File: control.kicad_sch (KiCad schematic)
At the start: 27 parts, among them J7 USB_C_Receptacle_USB2.0, J8 Conn_01x04_Male, J9 Conn_ARM_JTAG_SWD_10, U5 AMS1117-3.3, U6 STM32F042C4Tx, U7 USBLC6-2SC6

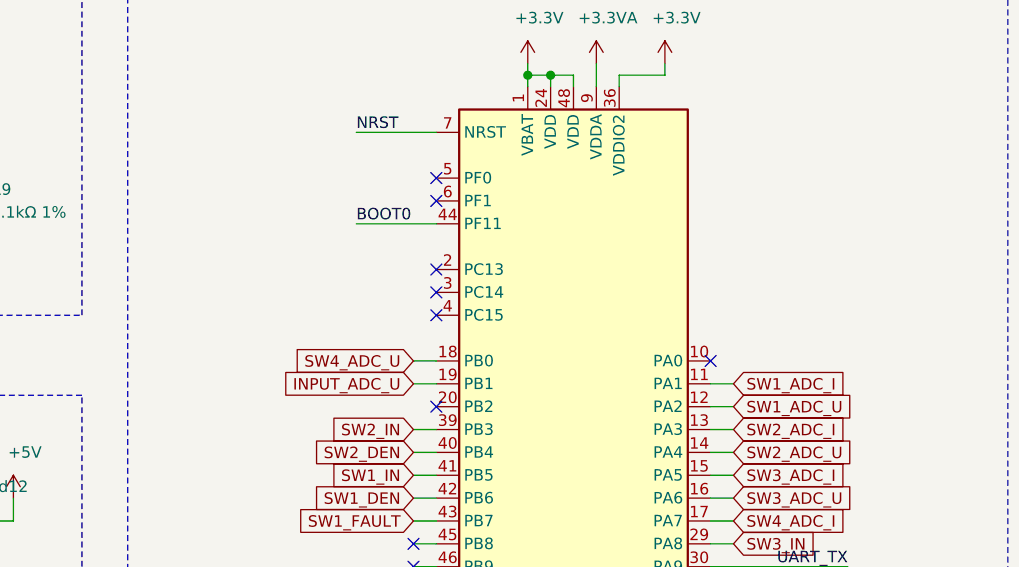
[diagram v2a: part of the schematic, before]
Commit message: add uC controlled status LED, improve filling zones, move LED closer to connectors
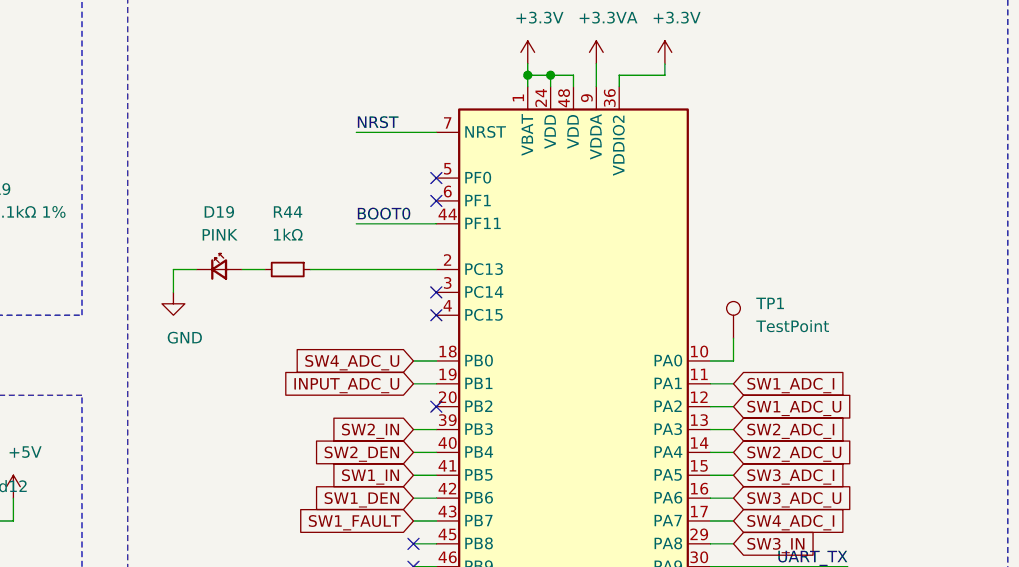
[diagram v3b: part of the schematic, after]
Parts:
- added D19: PINK, LED_SMD:LED_0603_1608Metric, symbol Device:LED_Small
- added R44: 1kΩ, Resistor_SMD:R_0603_1608Metric, symbol Device:R_Small
- added TP1: TestPoint, TestPoint:TestPoint_Pad_D1.0mm, symbol Connector:TestPoint
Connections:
- net GND: now also D19.1 (K)
- net at U6.10 (PA0): now also TP1.1
- net at U6.2 (PC13): now also R44.1
- new net: D19.2 (A), R44.2
- no-connect marks 15 -> 13
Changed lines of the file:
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@@
   (paper "A4")
   (title_block
+    (date "2020-11-09")
+    (rev "v0.1")
     (comment 4 "Author: Stefan Agner")
   )
@@
   (junction (at 209.55 66.04) (diameter 1.016) (color 0 0 0 0))
   (junction (at 212.09 142.24) (diameter 1.016) (color 0 0 0 0))
+  (no_connect (at 227.33 129.54))
+  (no_connect (at 100.33 127))
+  (no_connect (at 102.87 99.06))
+  (no_connect (at 100.33 124.46))
+  (no_connect (at 100.33 129.54))
+  (no_connect (at 102.87 83.82))
   (no_connect (at 46.99 57.15))
-  (no_connect (at 100.33 124.46))
-  (no_connect (at 100.33 127))
-  (no_connect (at 100.33 129.54))
+  (no_connect (at 102.87 96.52))
   (no_connect (at 46.99 59.69))
-  (no_connect (at 227.33 129.54))
   (no_connect (at 102.87 109.22))
-  (no_connect (at 102.87 99.06))
-  (no_connect (at 133.35 104.14))
-  (no_connect (at 102.87 93.98))
   (no_connect (at 102.87 86.36))
+  (no_connect (at 24.13 67.31))
   (no_connect (at 227.33 127))
-  (no_connect (at 102.87 83.82))
-  (no_connect (at 102.87 96.52))
-  (no_connect (at 24.13 67.31))
   (wire (pts (xy 21.59 173.99) (xy 33.02 173.99))
     (stroke (width 0) (type solid) (color 0 0 0 0))
@@
     (stroke (width 0) (type solid) (color 0 0 0 0))
   )
+  (wire (pts (xy 73.66 93.98) (xy 76.2 93.98))
+    (stroke (width 0) (type solid) (color 0 0 0 0))
+  )
+  (wire (pts (xy 73.66 96.52) (xy 73.66 93.98))
+    (stroke (width 0) (type solid) (color 0 0 0 0))
+  )
   (wire (pts (xy 74.93 31.75) (xy 74.93 29.21))
     (stroke (width 0) (type solid) (color 0 0 0 0))
@@
     (stroke (width 0) (type solid) (color 0 0 0 0))
   )
+  (wire (pts (xy 81.28 93.98) (xy 83.82 93.98))
+    (stroke (width 0) (type solid) (color 0 0 0 0))
+  )
   (wire (pts (xy 82.55 172.72) (xy 82.55 175.26))
     (stroke (width 0) (type solid) (color 0 0 0 0))
@@
     (stroke (width 0) (type solid) (color 0 0 0 0))
   )
+  (wire (pts (xy 88.9 93.98) (xy 102.87 93.98))
+    (stroke (width 0) (type solid) (color 0 0 0 0))
+  )
   (wire (pts (xy 93.98 31.75) (xy 99.06 31.75))
     (stroke (width 0) (type solid) (color 0 0 0 0))
@@
     (stroke (width 0) (type solid) (color 0 0 0 0))
   )
+  (wire (pts (xy 133.35 104.14) (xy 135.89 104.14))
+    (stroke (width 0) (type solid) (color 0 0 0 0))
+  )
   (wire (pts (xy 133.35 106.68) (xy 135.89 106.68))
     (stroke (width 0) (type solid) (color 0 0 0 0))
@@
   )
   (wire (pts (xy 134.62 172.72) (xy 139.7 172.72))
+    (stroke (width 0) (type solid) (color 0 0 0 0))
+  )
+  (wire (pts (xy 135.89 101.6) (xy 135.89 104.14))
     (stroke (width 0) (type solid) (color 0 0 0 0))
   )
@@
     )
   )
+  (symbol (lib_id "Connector:TestPoint") (at 135.89 101.6 0) (unit 1)
+    (in_bom yes) (on_board yes)
+    (property "Reference" "TP1" (id 0) (at 138.43 97.79 0)
+      (effects (font (size 1.27 1.27)) (justify left))
+    )
+    (property "Value" "TestPoint" (id 1) (at 138.43 100.33 0)
+      (effects (font (size 1.27 1.27)) (justify left))
+    )
+    (property "Footprint" "TestPoint:TestPoint_Pad_D1.0mm" (id 2) (at 140.97 101.6 0)
+      (effects (font (size 1.27 1.27)) hide)
+    )
+    (property "Datasheet" "~" (id 3) (at 140.97 101.6 0)
+      (effects (font (size 1.27 1.27)) hide)
+    )
+  )
   (symbol (lib_id "power:+3.3V") (at 34.29 119.38 0) (unit 1)
     (in_bom yes) (on_board yes)
@@
     )
   )
+  (symbol (lib_id "power:GND") (at 73.66 96.52 0) (unit 1)
+    (in_bom yes) (on_board yes)
+    (property "Reference" "#PWR0103" (id 0) (at 73.66 102.87 0)
+      (effects (font (size 1.27 1.27)) hide)
+    )
+    (property "Value" "GND" (id 1) (at 74.93 101.6 0))
+    (property "Footprint" "" (id 2) (at 73.66 96.52 0)
+      (effects (font (size 1.27 1.27)) hide)
+    )
+    (property "Datasheet" "" (id 3) (at 73.66 96.52 0)
+      (effects (font (size 1.27 1.27)) hide)
+    )
+  )
   (symbol (lib_id "power:GND") (at 82.55 185.42 0) (unit 1)
     (in_bom yes) (on_board yes)
@@
     )
   )
+  (symbol (lib_id "Device:R_Small") (at 86.36 93.98 270) (unit 1)
+    (in_bom yes) (on_board yes)
+    (property "Reference" "R44" (id 0) (at 86.36 87.63 90))
+    (property "Value" "1kΩ" (id 1) (at 86.36 90.17 90))
+    (property "Footprint" "Resistor_SMD:R_0603_1608Metric" (id 2) (at 86.36 93.98 0)
+      (effects (font (size 1.27 1.27)) hide)
+    )
+    (property "Datasheet" "~" (id 3) (at 86.36 93.98 0)
+      (effects (font (size 1.27 1.27)) hide)
+    )
+  )
   (symbol (lib_id "Device:R_Small") (at 91.44 172.72 90) (unit 1)
     (in_bom yes) (on_board yes)
@@
       (effects (font (size 1.27 1.27)) hide)
     )
+  )
+  (symbol (lib_id "Device:LED_Small") (at 78.74 93.98 0) (unit 1)
+    (in_bom yes) (on_board yes)
+    (property "Reference" "D19" (id 0) (at 78.74 87.63 0))
+    (property "Value" "PINK" (id 1) (at 78.74 90.17 0))
+    (property "Footprint" "LED_SMD:LED_0603_1608Metric" (id 2) (at 78.74 93.98 90)
+      (effects (font (size 1.27 1.27)) hide)
+    )
+    (property "Datasheet" "~" (id 3) (at 78.74 93.98 90)
+      (effects (font (size 1.27 1.27)) hide)
+    )
